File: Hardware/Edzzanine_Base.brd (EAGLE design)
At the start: 30.5 x 44.5 mm, 39 parts, among them U1 MIC5219 3.3V, U2 FTS31XS-U

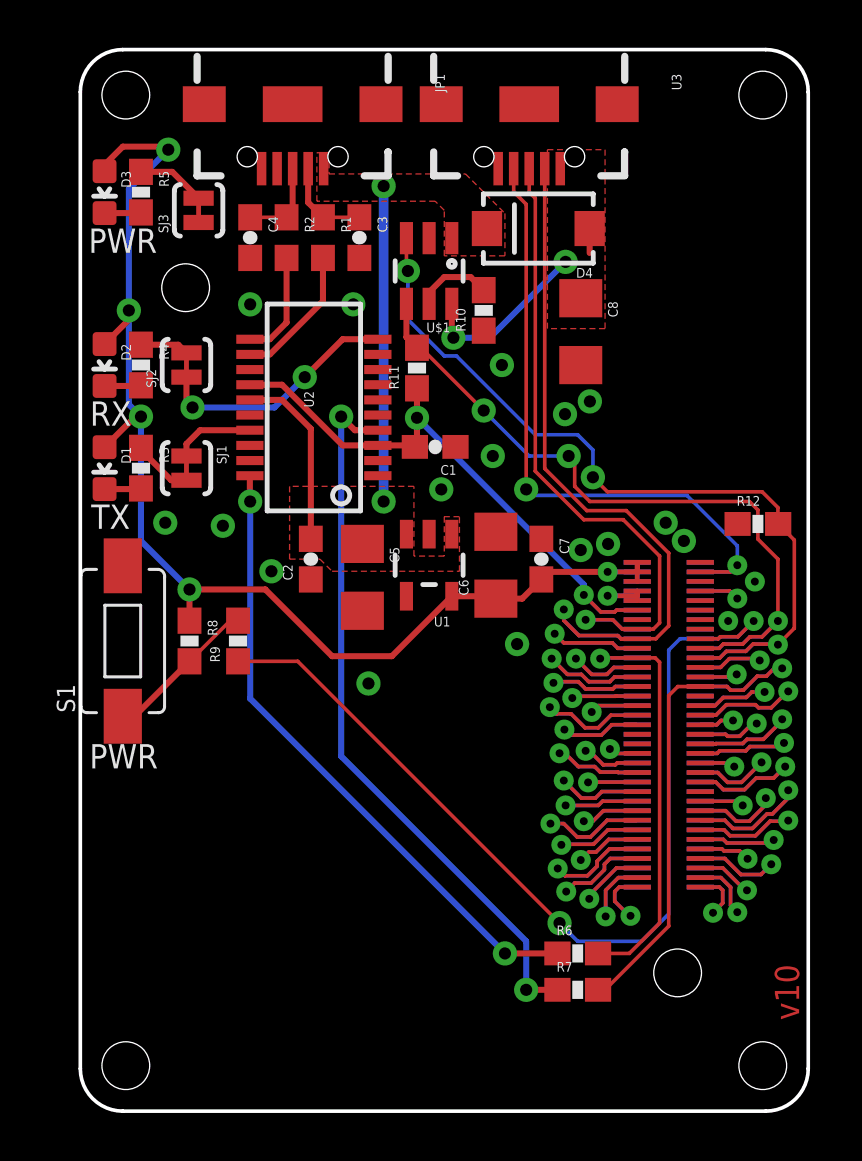
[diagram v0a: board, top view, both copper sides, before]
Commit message: changed out power supply for something more powerful. Added fiducials
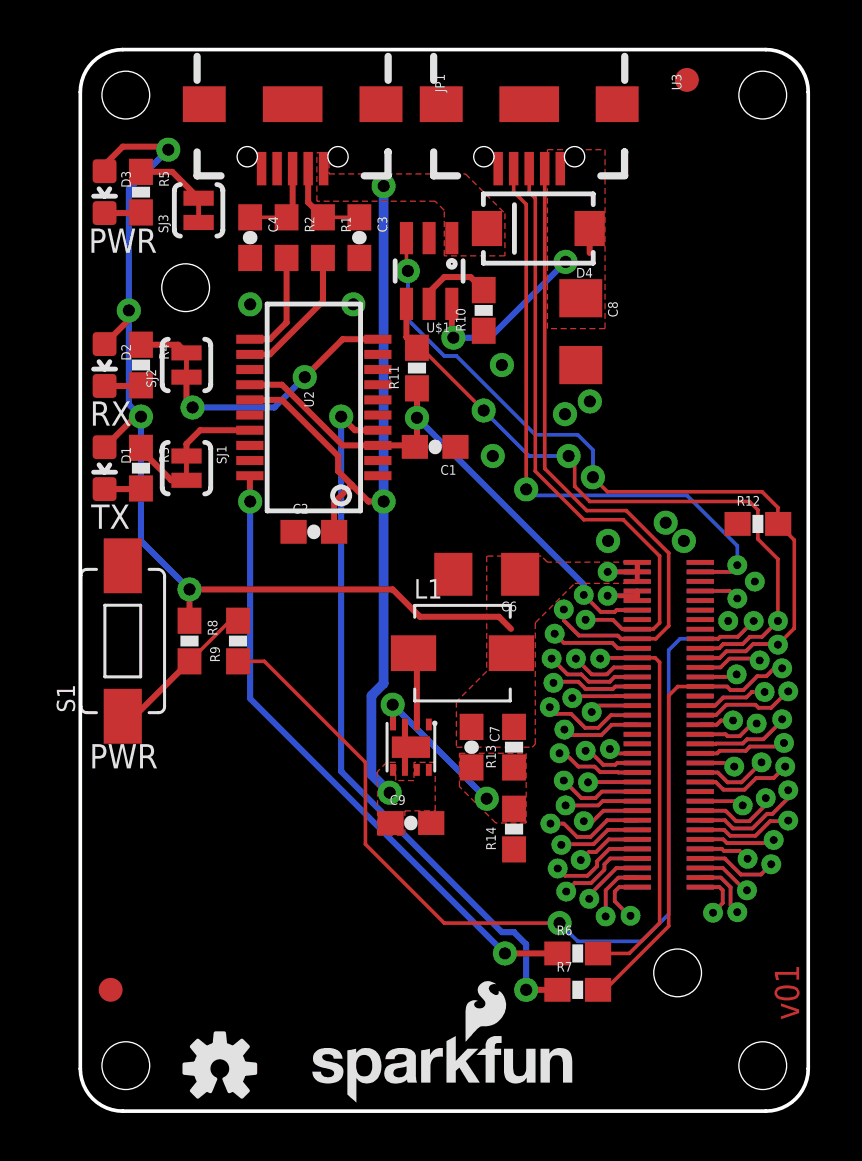
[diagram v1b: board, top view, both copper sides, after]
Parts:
- removed C5: 10uF, SparkFun-Capacitors:1206
- removed U1: MIC5219 3.3V, SparkFun-PowerIC:SOT23-5
- added C9: 4.7uF, SparkFun-Capacitors:0603-CAP
- added FID1, FID2: FIDUCIAL1X2, SparkFun-Aesthetics:FIDUCIAL-1X2
- added L1: (no value), SparkFun-Passives:INDUCTOR-SRP4020
- added LOGO1: SFE_LOGO_NAME_FLAME.1_INCH, SparkFun-Aesthetics:SFE_LOGO_NAME_FLAME_.1
- added LOGO4: OSHW-LOGOS, SparkFun-Aesthetics:OSHW-LOGO-S
- added R13: 680k, SparkFun-Resistors:0603-RES
- added R14: 120k, SparkFun-Resistors:0603-RES
- added U4: TPS62065, Testing:WSON-8-PAD
- C7: value 0.1uF -> 9.0pF
- moved C7 8.40 mm to (16.4, 15.2)
- moved C2 1.15 mm to (9.78, 24.3), turned to 0 degrees
- moved C6 0.54 mm to (17.0, 22.5), turned to 180 degrees
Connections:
- new net N$17: C7.2, R13.1, R14.2, U4.4
- new net N$19: L1.P$1, U4.2
- net 5V: now also C9.1, U4.5, U4.7, U4.8; no longer C5.1, U1.1, U1.3
- net GND: now also C9.2, R14.1, U4.1, U4.3, U4.6, U4.PAD; no longer C5.2, C7.1, U1.2
- net VSYS: now also C7.1, L1.P$2, R13.2; no longer C7.2, U1.5
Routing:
- net 5V: track 20.9 -> 35.9 mm, vias 2 -> 3
- net N$17: track 0.00 -> 6.58 mm, vias 0 -> 2
- net VSYS: track 53.3 -> 47.3 mm
- net N$19: track 0.00 -> 3.05 mm
- net GND: track 0.00 -> 2.11 mm, vias 18 -> 11
- net PWRBTN#: track 41.3 -> 43.3 mm
- added copper zone on layer 1, net N$17
- added copper zone on layer 1, net VSYS
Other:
- board text added: "v01"
- board text removed: "v10"

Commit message: moved USB connector to give room for larger cables
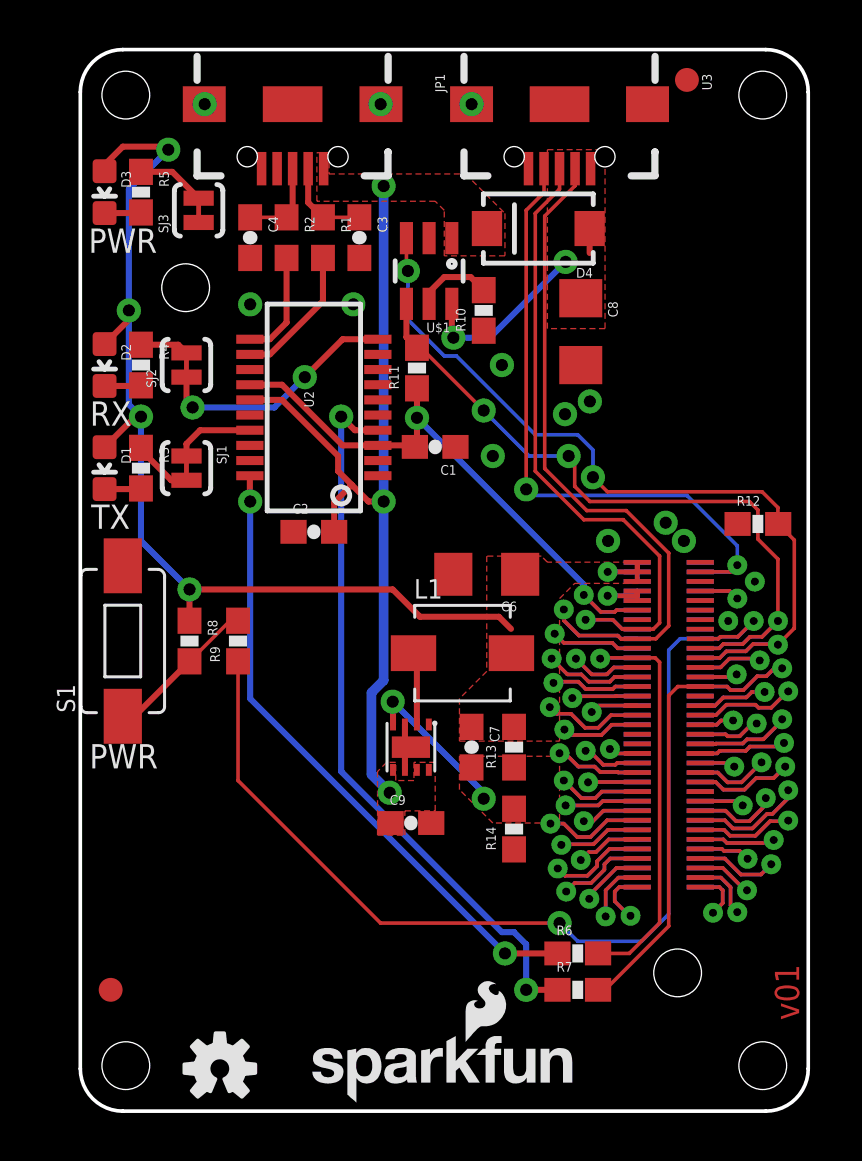
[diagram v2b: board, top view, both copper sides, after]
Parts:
- moved U3 1.27 mm to (20.1, 42.2)
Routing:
- net PWRBTN#: track 43.3 -> 44.0 mm
- net USB_DN: track 31.5 -> 32.0 mm
- net GND: vias 11 -> 14
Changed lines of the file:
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@@
 <setting verticaltext="up"/>
 </settings>
-<grid distance="0.05" unitdist="inch" unit="inch" style="lines" multiple="1" display="yes" altdistance="0.005" altunitdist="inch" altunit="inch"/>
+<grid distance="0.005" unitdist="inch" unit="inch" style="lines" multiple="1" display="yes" altdistance="0.005" altunitdist="inch" altunit="inch"/>
 <layers>
 <layer number="1" name="Top" color="4" fill="1" visible="yes" active="yes"/>
@@
 <text x="0.381" y="14.351" size="1.016" layer="21" font="vector" ratio="15" rot="SR0">PWR</text>
 <text x="8.89" y="43.18" size="1.4224" layer="22" font="vector" ratio="15" rot="MR0" align="center">CONSOLE</text>
-<text x="18.796" y="43.18" size="1.4224" layer="22" font="vector" ratio="15" rot="MR0" align="center">OTG</text>
+<text x="20.066" y="43.18" size="1.4224" layer="22" font="vector" ratio="15" rot="MR0" align="center">OTG</text>
 <text x="30.099" y="3.81" size="1.016" layer="1" font="vector" ratio="15" rot="R90">v01</text>
 </plain>
@@
 <attribute name="PROD_ID" value="RES-08698" x="6.604" y="19.685" size="1.778" layer="27" rot="R90" display="off"/>
 </element>
-<element name="U3" library="SparkFun-Connectors" package="USB-AB-MICRO-SMD_V03" value="" x="18.796" y="42.164" rot="R270">
-<attribute name="PROD_ID" value="CONN-11794" x="18.796" y="42.164" size="1.778" layer="27" rot="R270" display="off"/>
+<element name="U3" library="SparkFun-Connectors" package="USB-AB-MICRO-SMD_V03" value="" x="20.066" y="42.164" rot="R270">
+<attribute name="PROD_ID" value="CONN-11794" x="20.066" y="42.164" size="1.778" layer="27" rot="R270" display="off"/>
 </element>
 <element name="D4" library="SparkFun-DiscreteSemi" package="SMA-DIODE" value="" x="19.177" y="36.957" rot="R180">
@@
 <wire x1="13.593" y1="14.29" x2="13.593" y2="14.99" width="0.254" layer="1"/>
 <wire x1="13.593" y1="14.99" x2="13.843" y2="15.24" width="0.254" layer="1"/>
+<via x="16.383" y="42.164" extent="1-16" drill="0.508"/>
+<via x="12.573" y="42.164" extent="1-16" drill="0.508"/>
+<via x="5.207" y="42.164" extent="1-16" drill="0.508"/>
 </signal>
 <signal name="VSYS">
@@
 <contactref element="L1" pad="P$2"/>
 <polygon width="0.254" layer="1">
-<vertex x="15.748" y="15.24"/>
-<vertex x="18.923" y="15.24"/>
-<vertex x="19.05" y="15.367"/>
-<vertex x="19.05" y="20.447"/>
+<vertex x="15.875" y="15.494"/>
+<vertex x="20.066" y="15.494"/>
+<vertex x="20.066" y="21.463"/>
 <vertex x="20.701" y="22.098"/>
 <vertex x="23.368" y="22.098"/>
@@
 <vertex x="17.018" y="23.241"/>
 <vertex x="17.018" y="18.415"/>
-<vertex x="15.748" y="17.145"/>
+<vertex x="15.875" y="17.272"/>
 </polygon>
 <wire x1="4.572" y1="21.844" x2="13.081" y2="21.844" width="0.254" layer="1"/>
@@
 <wire x1="22.7332" y1="19.7798" x2="22.733" y2="19.78" width="0.1524" layer="1"/>
 <wire x1="22.733" y1="19.78" x2="22.638" y2="19.78" width="0.1524" layer="1"/>
-<wire x1="19.446" y1="39.464" x2="19.446" y2="39.482" width="0.1524" layer="1"/>
 <wire x1="24.638" y1="20.32" x2="24.0978" y2="19.7798" width="0.1524" layer="1"/>
 <wire x1="24.0978" y1="19.7798" x2="23.32" y2="19.7798" width="0.1524" layer="1"/>
 <wire x1="24.638" y1="20.32" x2="24.638" y2="23.368" width="0.1524" layer="1"/>
-<wire x1="19.446" y1="26.909" x2="19.446" y2="39.464" width="0.1524" layer="1"/>
+<wire x1="19.446" y1="37.48" x2="20.716" y2="38.75" width="0.1524" layer="1"/>
+<wire x1="20.716" y1="38.75" x2="20.716" y2="39.464" width="0.1524" layer="1"/>
 <wire x1="19.446" y1="26.909" x2="21.209" y2="25.146" width="0.1524" layer="1"/>
 <wire x1="21.209" y1="25.146" x2="22.86" y2="25.146" width="0.1524" layer="1"/>
 <wire x1="22.86" y1="25.146" x2="24.638" y2="23.368" width="0.1524" layer="1"/>
+<wire x1="19.446" y1="37.48" x2="19.446" y2="26.909" width="0.1524" layer="1"/>
 </signal>
 <signal name="USB_DP">
@@
 <wire x1="24.257" y1="20.447" x2="23.9898" y2="20.1798" width="0.1524" layer="1"/>
 <wire x1="23.32" y1="20.1798" x2="23.9898" y2="20.1798" width="0.1524" layer="1"/>
-<wire x1="19.05" y1="26.797" x2="19.05" y2="38.227" width="0.1524" layer="1"/>
-<wire x1="19.05" y1="38.227" x2="18.796" y2="38.481" width="0.1524" layer="1"/>
-<wire x1="18.796" y1="38.481" x2="18.796" y2="39.464" width="0.1524" layer="1"/>
+<wire x1="19.05" y1="26.797" x2="19.05" y2="37.592" width="0.1524" layer="1"/>
+<wire x1="19.05" y1="37.592" x2="20.066" y2="38.608" width="0.1524" layer="1"/>
+<wire x1="20.066" y1="38.608" x2="20.066" y2="39.464" width="0.1524" layer="1"/>
 <wire x1="19.05" y1="26.797" x2="21.082" y2="24.765" width="0.1524" layer="1"/>
 <wire x1="21.082" y1="24.765" x2="22.733" y2="24.765" width="0.1524" layer="1"/>
@@
 <wire x1="27.509" y1="23.672" x2="27.509" y2="22.86" width="0.1524" layer="16"/>
 <via x="18.669" y="26.035" extent="1-16" drill="0.508"/>
-<wire x1="18.669" y1="26.035" x2="18.669" y2="37.973" width="0.1524" layer="1"/>
-<wire x1="18.669" y1="37.973" x2="18.146" y2="38.496" width="0.1524" layer="1"/>
-<wire x1="18.146" y1="39.464" x2="18.146" y2="38.496" width="0.1524" layer="1"/>
+<wire x1="18.669" y1="26.035" x2="18.669" y2="37.719" width="0.1524" layer="1"/>
 <wire x1="25.4" y1="25.781" x2="18.923" y2="25.781" width="0.1524" layer="16"/>
 <wire x1="18.923" y1="25.781" x2="18.669" y2="26.035" width="0.1524" layer="16"/>
+<wire x1="18.669" y1="37.719" x2="19.416" y2="38.466" width="0.1524" layer="1"/>
+<wire x1="19.416" y1="38.466" x2="19.416" y2="39.464" width="0.1524" layer="1"/>
 </signal>
 <signal name="GP114_SPI_2_RXD">
@@
 <wire x1="6.692" y1="18.835" x2="6.604" y2="18.835" width="0.254" layer="1"/>
 <wire x1="20.828" y1="7.112" x2="23.495" y2="7.112" width="0.1524" layer="16"/>
-<wire x1="6.819" y1="18.835" x2="6.604" y2="18.835" width="0.254" layer="1"/>
-<wire x1="6.604" y1="18.835" x2="7.708" y2="18.835" width="0.1524" layer="1"/>
 <via x="20.066" y="7.874" extent="1-16" drill="0.508"/>
 <wire x1="20.066" y1="7.874" x2="20.828" y2="7.112" width="0.1524" layer="16"/>
-<wire x1="7.708" y1="18.835" x2="11.938" y2="14.605" width="0.1524" layer="1"/>
-<wire x1="11.938" y1="14.605" x2="11.938" y2="11.176" width="0.1524" layer="1"/>
-<wire x1="11.938" y1="11.176" x2="15.24" y2="7.874" width="0.1524" layer="1"/>
-<wire x1="15.24" y1="7.874" x2="20.066" y2="7.874" width="0.1524" layer="1"/>
+<wire x1="12.573" y1="7.874" x2="20.066" y2="7.874" width="0.1524" layer="1"/>
+<wire x1="6.604" y1="18.835" x2="6.604" y2="13.843" width="0.1524" layer="1"/>
+<wire x1="6.604" y1="13.843" x2="12.573" y2="7.874" width="0.1524" layer="1"/>
 </signal>
 <signal name="V_BAT_BKUP">
@@
 <vertex x="12.446" y="14.224"/>
 </polygon>
-<wire x1="12.7" y1="25.527" x2="12.7" y2="17.907" width="0.4064" layer="16"/>
-<wire x1="12.7" y1="17.907" x2="12.192" y2="17.399" width="0.4064" layer="16"/>
-<wire x1="12.192" y1="17.399" x2="12.192" y2="14.097" width="0.4064" layer="16"/>
+<wire x1="12.7" y1="25.527" x2="12.7" y2="18.034" width="0.4064" layer="16"/>
+<wire x1="12.7" y1="18.034" x2="12.192" y2="17.526" width="0.4064" layer="16"/>
+<wire x1="12.192" y1="17.526" x2="12.192" y2="14.097" width="0.4064" layer="16"/>
 <via x="12.954" y="13.335" extent="1-16" drill="0.508"/>
 <wire x1="12.192" y1="14.097" x2="12.954" y2="13.335" width="0.4064" layer="16"/>
@@
 <contactref element="U4" pad="4"/>
 <polygon width="0.254" layer="1">
-<vertex x="15.875" y="14.986"/>
-<vertex x="18.669" y="14.986"/>
-<vertex x="18.669" y="12.065"/>
-<vertex x="17.399" y="12.065"/>
-<vertex x="15.875" y="13.589"/>
+<vertex x="15.875" y="14.859"/>
+<vertex x="20.066" y="14.859"/>
+<vertex x="20.066" y="12.065"/>
+<vertex x="17.272" y="12.065"/>
+<vertex x="15.875" y="13.462"/>
 </polygon>
-<wire x1="13.093" y1="16.19" x2="13.093" y2="17.006" width="0.254" layer="1"/>
-<wire x1="13.093" y1="17.006" x2="13.081" y2="17.018" width="0.254" layer="1"/>
-<via x="13.081" y="17.018" extent="1-16" drill="0.508"/>
-<wire x1="13.081" y1="17.018" x2="17.018" y2="13.081" width="0.254" layer="16"/>
-<via x="17.018" y="13.081" extent="1-16" drill="0.508"/>
-<wire x1="17.018" y1="13.081" x2="17.145" y2="13.208" width="0.254" layer="1"/>
+<wire x1="13.093" y1="17.133" x2="13.081" y2="17.145" width="0.254" layer="1"/>
+<via x="13.081" y="17.145" extent="1-16" drill="0.508"/>
+<via x="16.891" y="13.081" extent="1-16" drill="0.508"/>
+<wire x1="13.093" y1="17.133" x2="13.093" y2="16.19" width="0.254" layer="1"/>
+<wire x1="16.891" y1="13.081" x2="16.891" y2="13.335" width="0.254" layer="16"/>
+<wire x1="16.891" y1="13.335" x2="13.081" y2="17.145" width="0.254" layer="16"/>
 </signal>
 <signal name="N$19">
@@
 </signal>
 </signals>
+<errors>
+</errors>
 </board>
 </drawing>
